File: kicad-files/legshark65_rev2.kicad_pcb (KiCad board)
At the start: 2 copper layers, 285.8 x 97 mm, 199 parts, among them J1 ARM JTAG, SW1 K2-1187SQ-A4SW-06, SW2 PCM12SMTR, T2 53261-0471, U1 STM32F411CEU6, U2 MCP1700T-3302E/TT, U3 AT24C256C-SSHL-T, Y1 TAXM8M4RFDCET2T

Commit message: Started routing cols
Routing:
- net col12: track 0.00 -> 86.1 mm
- net col2: track 0.00 -> 86.0 mm
- net col6: track 0.00 -> 86.0 mm
- net col13: track 0.00 -> 84.5 mm
- net col1: track 0.00 -> 82.8 mm
- net col4: track 0.00 -> 81.8 mm
- net col0: track 0.00 -> 80.4 mm
- net col5: track 0.00 -> 78.0 mm
- net col7: track 0.00 -> 76.5 mm
- net col3: track 0.00 -> 76.5 mm
- net col11: track 0.00 -> 76.4 mm
- net col9: track 0.00 -> 76.4 mm
- net col14: track 0.00 -> 67.9 mm
- net col10: track 0.00 -> 62.2 mm
- net Net-(D_71-A): track 0.00 -> 15.0 mm
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
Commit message: routed the hard wire through the MCU
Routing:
- net col8: track 9.61 -> 109.1 mm
- net 3V3: track 36.5 -> 16.6 mm
- net Net-(D_52-A): track 0.00 -> 14.8 mm
- net row2: track 247.7 -> 244.8 mm
- net BOOT0: track 240.8 -> 242.5 mm
- net Net-(U1-PB7--I2C1_SDA): track 25.8 -> 27.2 mm
- net Net-(U1-PB6--I2C1_SCL): track 26.9 -> 28.1 mm
- net col0: track 80.4 -> 81.3 mm
- net unconnected-(U1-PA2-Pad12): track 7.45 -> 8.00 mm
- net unconnected-(U1-PA3-Pad13): track 9.48 -> 9.18 mm, vias 0 -> 1
- net GND: vias 11 -> 13

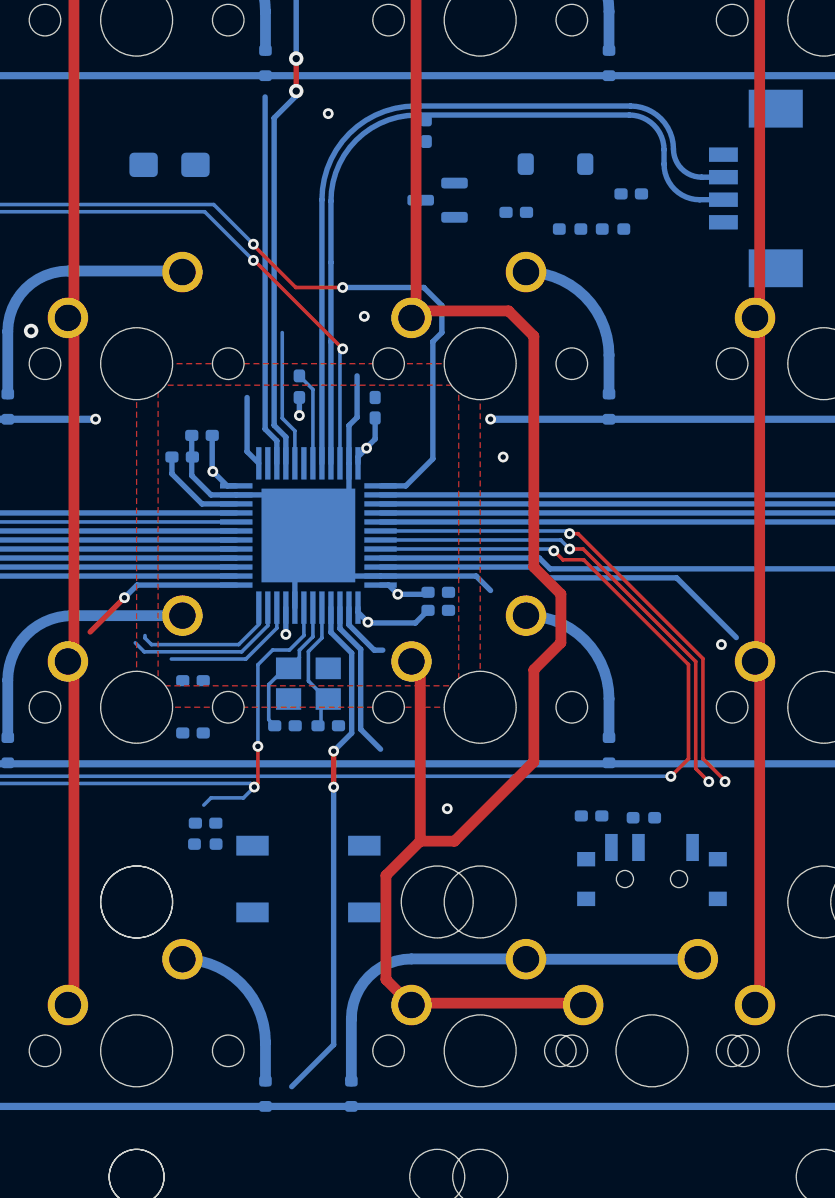
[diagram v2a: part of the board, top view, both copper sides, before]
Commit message: Made the pours correct distance
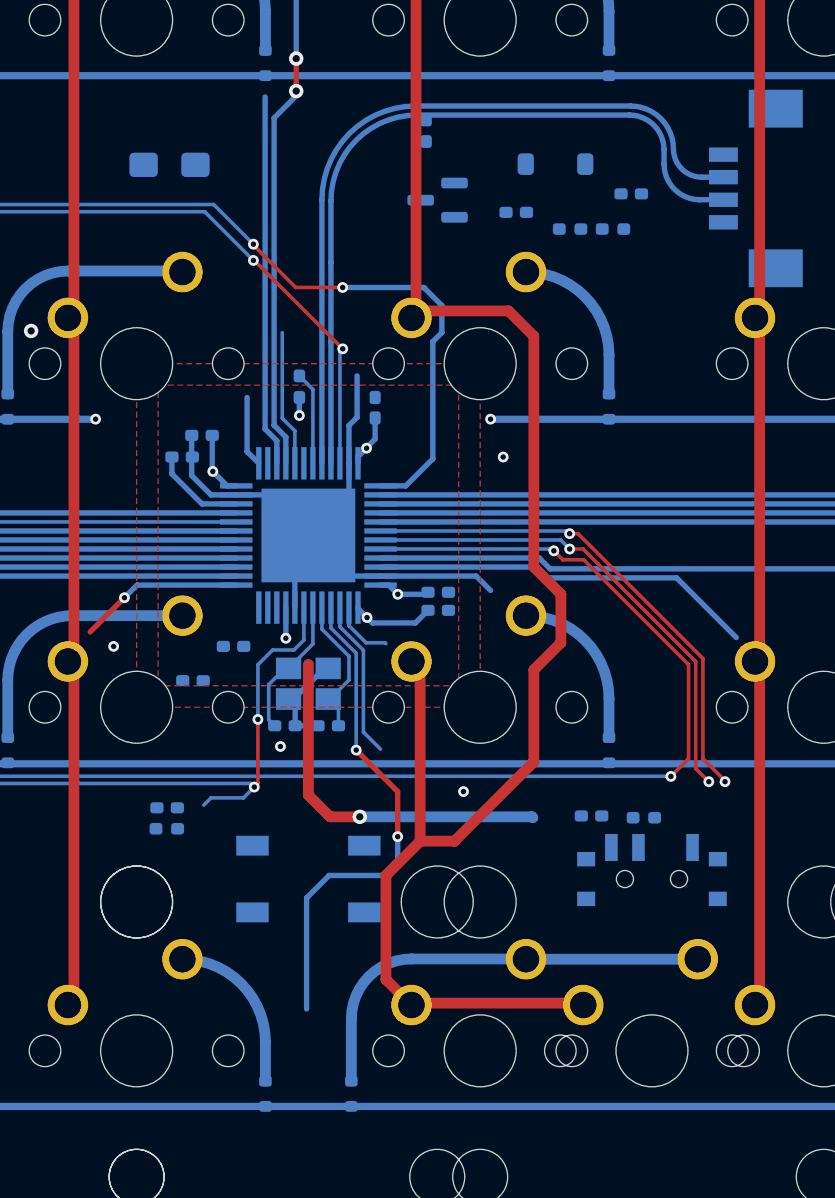
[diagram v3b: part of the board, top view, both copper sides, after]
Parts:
- moved C13 5.30 mm to (148.2, 63.3)
- moved R11 2.30 mm to (144.5, 73.4)
- moved C7 2.30 mm to (144.6, 72.2)
- turned C2 to 180 degrees
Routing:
- net 3V3: track 16.6 -> 36.9 mm, vias 6 -> 7
- net unconnected-(U1-PA1-Pad11): track 9.16 -> 0.00 mm
- net unconnected-(U1-PA2-Pad12): track 8.00 -> 0.00 mm
- net unconnected-(U1-PA0-WKUP-Pad10): track 7.70 -> 0.00 mm
- net GND: track 35.7 -> 41.5 mm, vias 13 -> 12
- net unconnected-(U1-PC15/OSC32_OUT-Pad4): track 28.4 -> 27.6 mm

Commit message: Added connections to col and row
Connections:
- U1 pad 13: unconnected-(U1-PA3-Pad13) -> col7
- U1 pad 14: unconnected-(U1-PA4-Pad14) -> col6
- U1 pad 15: unconnected-(U1-PA5-Pad15) -> col5
- U1 pad 16: unconnected-(U1-PA6-Pad16) -> col4
- U1 pad 17: unconnected-(U1-PA7-Pad17) -> col3
- U1 pad 18: unconnected-(U1-PB0-Pad18) -> col2
- U1 pad 19: unconnected-(U1-PB1-Pad19) -> col1
- U1 pad 2: unconnected-(U1-PC13-Pad2) -> col8
- U1 pad 21: unconnected-(U1-PB10-Pad21) -> col0
- U1 pad 25: unconnected-(U1-PB12-Pad25) -> row2
- U1 pad 27: unconnected-(U1-PB14-Pad27) -> row1
- U1 pad 28: unconnected-(U1-PB15/SPI2_MOSI-Pad28) -> row0
- U1 pad 3: unconnected-(U1-PC14/OSC32_IN-Pad3) -> row3
- U1 pad 38: unconnected-(U1-PA15-Pad38) -> col14
- U1 pad 39: unconnected-(U1-PB3-Pad39) -> col13
- U1 pad 4: unconnected-(U1-PC15/OSC32_OUT-Pad4) -> row4
- U1 pad 40: unconnected-(U1-PB4-Pad40) -> col12
- U1 pad 41: unconnected-(U1-PB5-Pad41) -> col11
- U1 pad 45: unconnected-(U1-PB8-Pad45) -> col10
- U1 pad 46: unconnected-(U1-PB9-Pad46) -> col9
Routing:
- net unconnected-(U1-PB10-Pad21): track 148.5 -> 0.00 mm
- net col0: track 81.3 -> 229.3 mm
- net col1: track 82.8 -> 209.7 mm
- net unconnected-(U1-PB1-Pad19): track 126.0 -> 0.00 mm
- net col14: track 67.9 -> 186.3 mm
- net unconnected-(U1-PA15-Pad38): track 118.1 -> 0.00 mm
- net col2: track 86.0 -> 192.5 mm
- net unconnected-(U1-PB0-Pad18): track 105.5 -> 0.00 mm
- net col13: track 84.5 -> 183.8 mm
- net unconnected-(U1-PB3-Pad39): track 98.8 -> 0.00 mm
- net col3: track 76.5 -> 163.7 mm
- net unconnected-(U1-PA7-Pad17): track 83.7 -> 0.00 mm
- net col12: track 86.1 -> 166.2 mm
- net unconnected-(U1-PB4-Pad40): track 79.5 -> 0.00 mm
- net col4: track 81.8 -> 150.0 mm
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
